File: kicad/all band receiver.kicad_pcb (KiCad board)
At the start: 2 copper layers, 77.9 x 29.5 mm, 34 parts, among them J1 AudioJack3_SwitchT, J2 Conn_01x01_Socket, J3 Conn_01x02_Socket, Q1 2N4401, U1 LM386

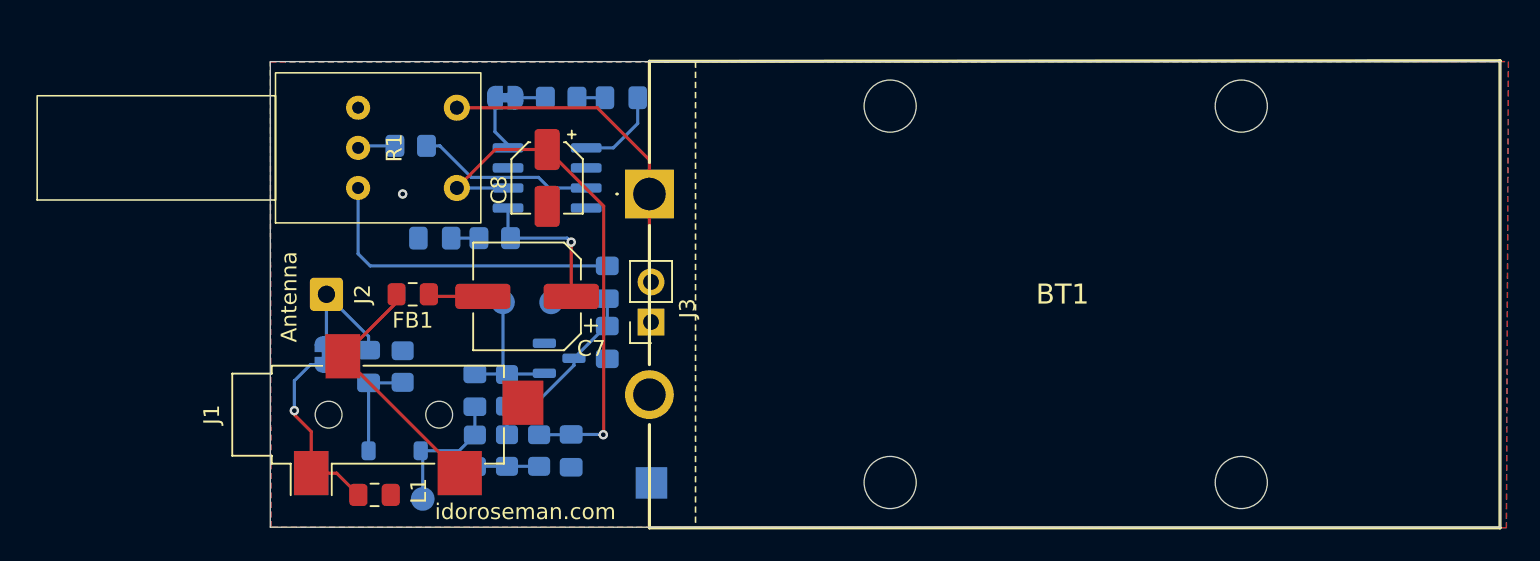
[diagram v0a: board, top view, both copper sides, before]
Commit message: moved (almost) all smt components to bottom side so manufacturing is cheaper. chanded audio connector on upper side to thruhole for easy soldering
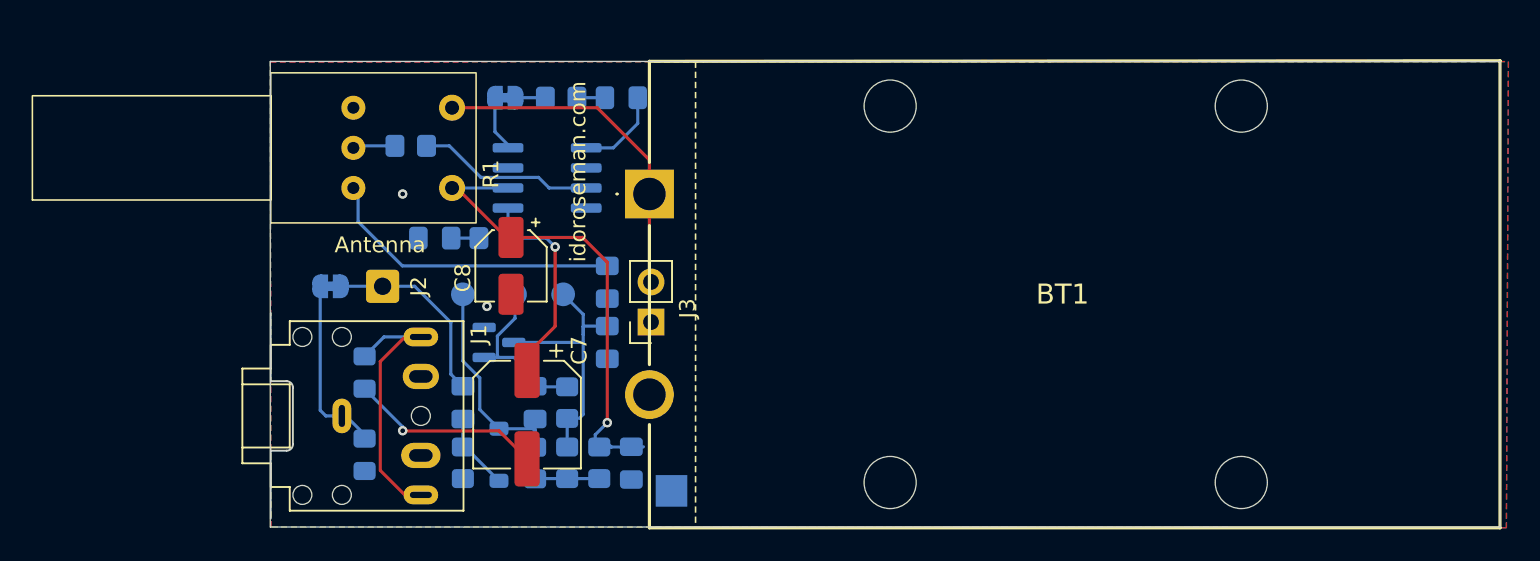
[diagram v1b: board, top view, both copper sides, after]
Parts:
- FB1, L1: moved to B.Cu
- J1: value AudioJack3_SwitchT -> AudioJack3_SwitchTR; footprint Connector_Audio:Jack_3.5mm_CUI_SJ-3524-SMT_Horizontal -> Connector_Audio:Jack_3.5mm_CUI_SJ1-3525N_Horizontal
- moved TP1 13.2 mm to (112.3, 65.5)
- moved C7 7.49 mm to (116.3, 73.2), turned to -90 degrees
- moved R2 7.19 mm to (112.3, 76.2), turned to -90 degrees
- moved D1 6.61 mm to (114.6, 75.7), turned to 90 degrees
- moved C1 6.39 mm to (112.3, 72.4)
- moved C8 6.02 mm to (115.3, 63.7)
- moved FB1 5.82 mm to (106.0, 70.5), turned to 90 degrees
- moved JP2 4.33 mm to (103.9, 65.0), turned to 180 degrees
- moved Q1 3.94 mm to (114.6, 68.6)
- moved C2 3.89 mm to (116.8, 72.4)
- moved C5 3.89 mm to (122.9, 76.2)
- moved R4 3.89 mm to (118.9, 72.4)
- moved R5 3.89 mm to (120.9, 76.2)
- moved R6 3.89 mm to (118.9, 76.2)
- moved R3 3.89 mm to (116.8, 76.2)
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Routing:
- net Net-(C7-Pad2): track 3.47 -> 12.3 mm, vias 0 -> 1
- net Net-(D1-A): track 8.72 -> 13.6 mm
- net +BATT: track 33.7 -> 29.0 mm
- net /AUX_ANT: track 7.80 -> 12.3 mm
- net Net-(C7-Pad1): track 9.35 -> 13.6 mm
- net Net-(D1-K): track 6.47 -> 4.86 mm
- net Net-(FB1-Pad2): track 15.8 -> 14.3 mm
- net Net-(C4-Pad2): track 20.3 -> 19.1 mm
- net Net-(JP2-B): track 12.3 -> 11.3 mm, vias 1 -> 0
- net Net-(Q1-B): track 9.60 -> 10.5 mm
- net GND: track 0.20 -> 0.00 mm, vias 1 -> 2

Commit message: production
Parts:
- J1: value AudioJack3_SwitchTR -> CUI_SJ1-3525N
- J2: footprint Connector_Wire:SolderWire-0.5sqmm_1x01_D0.9mm_OD2.1mm -> Connector_PinHeader_2.54mm:PinHeader_1x01_P2.54mm_Horizontal
- R1: value ~ -> P091S-QC15BR
- moved TP4 2.29 mm to (125.5, 75.7)
- moved J2 1.33 mm to (108.5, 65.0), turned to 180 degrees
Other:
- board size 77.9 x 29.5 mm -> 26.9 x 29.5 mm
- board text added: "S/N"
